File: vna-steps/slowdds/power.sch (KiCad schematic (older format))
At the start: 13 parts

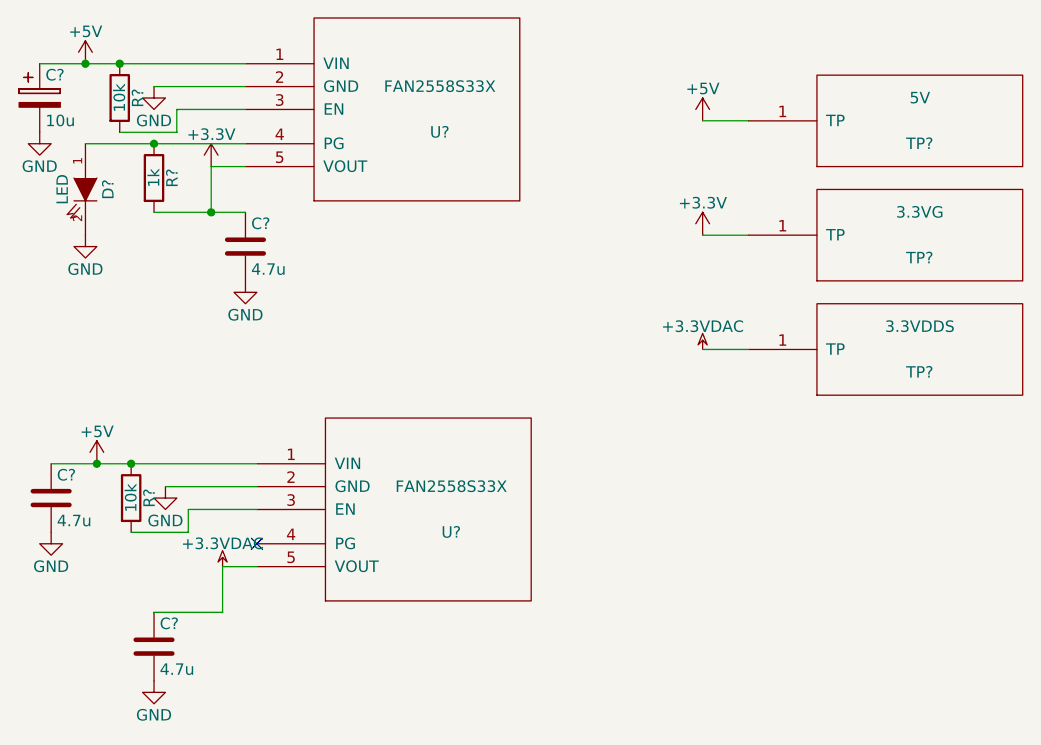
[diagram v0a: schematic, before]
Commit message: slowdds layout completed. images + schematics generated. ZIP file scripts added and documented in README. slowdds gerbers generated + zipped.
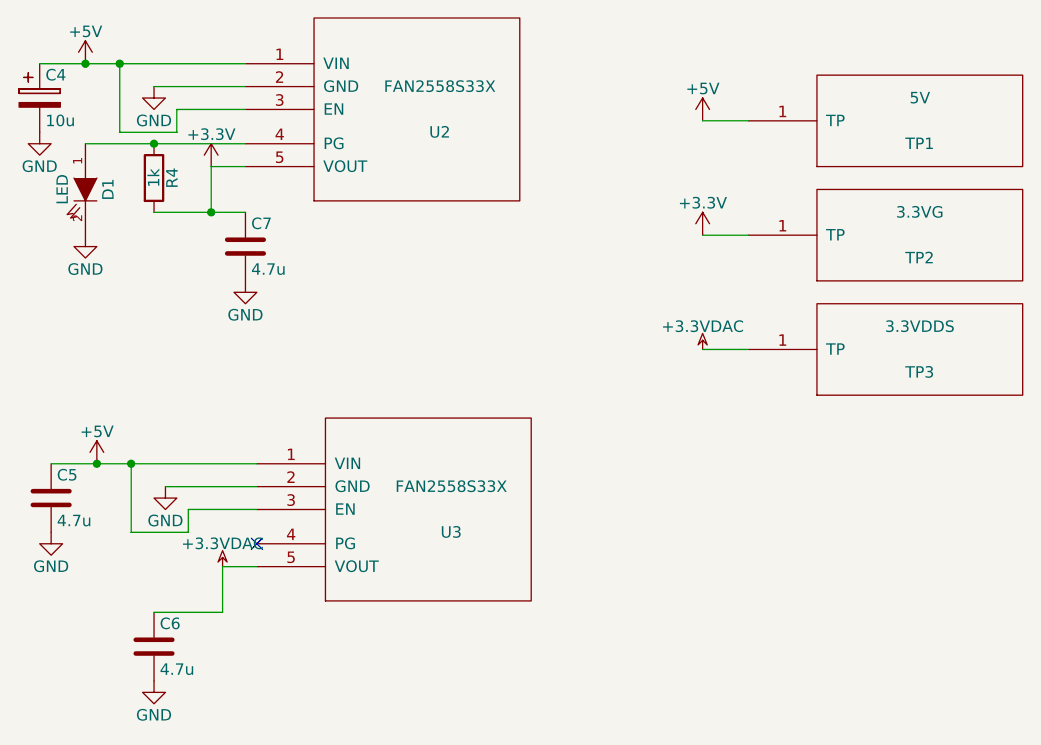
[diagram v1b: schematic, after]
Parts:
- removed R? (x2): 10k, symbol R
- C4: renamed from C?; footprint (none) -> Capacitors_Tantalum_SMD:TantalC_SizeA_EIA-3216_Reflow
- C5, C6, C7: renamed from C?; footprint (none) -> Capacitors_SMD:C_0603
- D1: renamed from D?; footprint (none) -> LEDs:LED-0603
- R4: renamed from R?; footprint (none) -> Resistors_SMD:R_0402
- TP1, TP2, TP3: renamed from TP?; footprint MODULE -> bce:TP
- U2, U3: renamed from U?; footprint MODULE -> Housings_SOT-23_SOT-143_TSOT-6:SOT-23-5
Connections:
- net +5V: now also U2.3 (EN), U3.3 (EN)
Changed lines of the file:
@@
 $EndDescr
 $Comp
-L GND #PWR?
+L GND #PWR011
 U 1 1 55851E90
 P 3750 3300
-F 0 "#PWR?" H 3750 3050 50  0001 C CNN
+F 0 "#PWR011" H 3750 3050 50  0001 C CNN
 F 1 "GND" H 3750 3150 50  0000 C CNN
 F 2 "" H 3750 3300 60  0000 C CNN
@@
 Connection ~ 3600 3000
 $Comp
-L C C?
+L C C7
 U 1 1 55851DEA
 P 3750 3150
-F 0 "C?" H 3775 3250 50  0000 L CNN
+F 0 "C7" H 3775 3250 50  0000 L CNN
 F 1 "4.7u" H 3775 3050 50  0000 L CNN
-F 2 "" H 3788 3000 30  0000 C CNN
+F 2 "Capacitors_SMD:C_0603" H 3788 3000 30  0001 C CNN
 F 3 "" H 3750 3150 60  0000 C CNN
 	1    3750 3150
@@
 $EndComp
 $Comp
-L GND #PWR?
+L GND #PWR012
 U 1 1 55851DC9
 P 2850 2650
-F 0 "#PWR?" H 2850 2400 50  0001 C CNN
+F 0 "#PWR012" H 2850 2400 50  0001 C CNN
 F 1 "GND" H 2850 2500 50  0000 C CNN
 F 2 "" H 2850 2650 60  0000 C CNN
@@
 	3350 2450 3750 2450
 $Comp
-L GND #PWR?
+L GND #PWR013
 U 1 1 55851D93
 P 3050 3100
-F 0 "#PWR?" H 3050 2850 50  0001 C CNN
+F 0 "#PWR013" H 3050 2850 50  0001 C CNN
 F 1 "GND" H 3050 2950 50  0000 C CNN
 F 2 "" H 3050 3100 60  0000 C CNN
@@
 Connection ~ 3350 2700
 $Comp
-L LED D?
+L LED D1
 U 1 1 55851CDF
 P 3050 2900
-F 0 "D?" H 3050 3000 50  0000 C CNN
+F 0 "D1" H 3050 3000 50  0000 C CNN
 F 1 "LED" H 3050 2800 50  0000 C CNN
-F 2 "" H 3050 2900 60  0000 C CNN
+F 2 "LEDs:LED-0603" H 3050 2900 60  0001 C CNN
 F 3 "" H 3050 2900 60  0000 C CNN
 	1    3050 2900
@@
 	3600 3000 3600 2800
 Wire Wire Line
-	3350 3000 3600 3000
-Wire Wire Line
-	3600 3000 3750 3000
-Wire Wire Line
-	3050 2700 3350 2700
-Wire Wire Line
-	3350 2700 3750 2700
-$Comp
-L R R?
+	3350 3000 3750 3000
+Wire Wire Line
+	3050 2700 3750 2700
+$Comp
+L R R4
 U 1 1 55851C98
 P 3350 2850
-F 0 "R?" V 3430 2850 50  0000 C CNN
+F 0 "R4" V 3430 2850 50  0000 C CNN
 F 1 "1k" V 3350 2850 50  0000 C CNN
-F 2 "" V 3280 2850 30  0000 C CNN
+F 2 "Resistors_SMD:R_0402" V 3280 2850 30  0001 C CNN
 F 3 "" H 3350 2850 30  0000 C CNN
 	1    3350 2850
@@
 	3600 2800 3750 2800
 $Comp
-L +3.3V #PWR?
+L +3.3V #PWR014
 U 1 1 55851C32
 P 3600 2800
-F 0 "#PWR?" H 3600 2650 50  0001 C CNN
+F 0 "#PWR014" H 3600 2650 50  0001 C CNN
 F 1 "+3.3V" H 3600 2940 50  0000 C CNN
 F 2 "" H 3600 2800 60  0000 C CNN
@@
 $EndComp
 $Comp
-L GND #PWR?
+L GND #PWR015
 U 1 1 55851BFD
 P 3350 2450
-F 0 "#PWR?" H 3350 2200 50  0001 C CNN
+F 0 "#PWR015" H 3350 2200 50  0001 C CNN
 F 1 "GND" H 3350 2300 50  0000 C CNN
 F 2 "" H 3350 2450 60  0000 C CNN
@@
 Connection ~ 3050 2350
 Wire Wire Line
-	2850 2350 3050 2350
-Wire Wire Line
-	3050 2350 3200 2350
-Wire Wire Line
-	3200 2350 3750 2350
-$Comp
-L R R?
-U 1 1 55851B9B
-P 3200 2500
-F 0 "R?" V 3280 2500 50  0000 C CNN
-F 1 "10k" V 3200 2500 50  0000 C CNN
-F 2 "" V 3130 2500 30  0000 C CNN
-F 3 "" H 3200 2500 30  0000 C CNN
-	1    3200 2500
-	1    0    0    -1
-$EndComp
-$Comp
-L +5V #PWR?
+	2850 2350 3750 2350
+$Comp
+L +5V #PWR016
 U 1 1 55851B85
 P 3050 2350
-F 0 "#PWR?" H 3050 2200 50  0001 C CNN
+F 0 "#PWR016" H 3050 2200 50  0001 C CNN
 F 1 "+5V" H 3050 2490 50  0000 C CNN
 F 2 "" H 3050 2350 60  0000 C CNN
@@
 $EndComp
 $Comp
-L CP C?
+L CP C4
 U 1 1 55851B48
 P 2850 2500
-F 0 "C?" H 2875 2600 50  0000 L CNN
+F 0 "C4" H 2875 2600 50  0000 L CNN
 F 1 "10u" H 2875 2400 50  0000 L CNN
-F 2 "" H 2888 2350 30  0000 C CNN
+F 2 "Capacitors_Tantalum_SMD:TantalC_SizeA_EIA-3216_Reflow" H 2888 2350 30  0001 C CNN
 F 3 "" H 2850 2500 60  0000 C CNN
 	1    2850 2500
@@
 $EndComp
 $Comp
-L FAN2558S33X U?
+L FAN2558S33X U2
 U 1 1 55851B19
 P 4500 2550
-F 0 "U?" H 4600 2450 50  0000 C CNN
+F 0 "U2" H 4600 2450 50  0000 C CNN
 F 1 "FAN2558S33X" H 4600 2650 50  0000 C CNN
-F 2 "MODULE" H 4500 2200 50  0001 C CNN
+F 2 "Housings_SOT-23_SOT-143_TSOT-6:SOT-23-5" H 4500 2200 50  0001 C CNN
 F 3 "DOCUMENTATION" H 4500 2850 50  0001 C CNN
 	1    4500 2550
@@
 $EndComp
 $Comp
-L GND #PWR?
+L GND #PWR017
 U 1 1 558520FF
 P 3350 5050
-F 0 "#PWR?" H 3350 4800 50  0001 C CNN
+F 0 "#PWR017" H 3350 4800 50  0001 C CNN
 F 1 "GND" H 3350 4900 50  0000 C CNN
 F 2 "" H 3350 5050 60  0000 C CNN
@@
 $EndComp
 $Comp
-L C C?
+L C C6
 U 1 1 55852106
 P 3350 4900
-F 0 "C?" H 3375 5000 50  0000 L CNN
+F 0 "C6" H 3375 5000 50  0000 L CNN
 F 1 "4.7u" H 3375 4800 50  0000 L CNN
-F 2 "" H 3388 4750 30  0000 C CNN
+F 2 "Capacitors_SMD:C_0603" H 3388 4750 30  0001 C CNN
 F 3 "" H 3350 4900 60  0000 C CNN
 	1    3350 4900
@@
 $EndComp
 $Comp
-L GND #PWR?
+L GND #PWR018
 U 1 1 5585210C
 P 2900 4400
-F 0 "#PWR?" H 2900 4150 50  0001 C CNN
+F 0 "#PWR018" H 2900 4150 50  0001 C CNN
 F 1 "GND" H 2900 4250 50  0000 C CNN
 F 2 "" H 2900 4400 60  0000 C CNN
@@
 	3650 4550 3800 4550
 $Comp
-L GND #PWR?
+L GND #PWR019
 U 1 1 55852130
 P 3400 4200
-F 0 "#PWR?" H 3400 3950 50  0001 C CNN
+F 0 "#PWR019" H 3400 3950 50  0001 C CNN
 F 1 "GND" H 3400 4050 50  0000 C CNN
 F 2 "" H 3400 4200 60  0000 C CNN
@@
 Connection ~ 3100 4100
 Wire Wire Line
-	2900 4100 3100 4100
-Wire Wire Line
-	3100 4100 3250 4100
-Wire Wire Line
-	3250 4100 3800 4100
-$Comp
-L R R?
-U 1 1 5585213C
-P 3250 4250
-F 0 "R?" V 3330 4250 50  0000 C CNN
-F 1 "10k" V 3250 4250 50  0000 C CNN
-F 2 "" V 3180 4250 30  0000 C CNN
-F 3 "" H 3250 4250 30  0000 C CNN
-	1    3250 4250
-	1    0    0    -1
-$EndComp
-$Comp
-L +5V #PWR?
+	2900 4100 3800 4100
+$Comp
+L +5V #PWR020
 U 1 1 55852142
 P 3100 4100
-F 0 "#PWR?" H 3100 3950 50  0001 C CNN
+F 0 "#PWR020" H 3100 3950 50  0001 C CNN
 F 1 "+5V" H 3100 4240 50  0000 C CNN
 F 2 "" H 3100 4100 60  0000 C CNN
@@
 $EndComp
 $Comp
-L FAN2558S33X U?
+L FAN2558S33X U3
 U 1 1 5585214E
 P 4550 4300
-F 0 "U?" H 4650 4200 50  0000 C CNN
+F 0 "U3" H 4650 4200 50  0000 C CNN
 F 1 "FAN2558S33X" H 4650 4400 50  0000 C CNN
-F 2 "MODULE" H 4550 3950 50  0001 C CNN
+F 2 "Housings_SOT-23_SOT-143_TSOT-6:SOT-23-5" H 4550 3950 50  0001 C CNN
 F 3 "DOCUMENTATION" H 4550 4600 50  0001 C CNN
 	1    4550 4300
@@
 $EndComp
 $Comp
-L TP TP?
+L TP TP1
 U 1 1 558521CE
 P 6700 2600
-F 0 "TP?" H 6700 2500 50  0000 C CNN
+F 0 "TP1" H 6700 2500 50  0000 C CNN
 F 1 "5V" H 6700 2700 50  0000 C CNN
-F 2 "MODULE" H 6450 2450 50  0001 C CNN
+F 2 "bce:TP" H 6450 2450 50  0001 C CNN
 F 3 "DOCUMENTATION" H 6700 2600 50  0001 C CNN
 	1    6700 2600
@@
 $EndComp
 $Comp
-L TP TP?
+L TP TP2
 U 1 1 55852299
 P 6700 3100
-F 0 "TP?" H 6700 3000 50  0000 C CNN
+F 0 "TP2" H 6700 3000 50  0000 C CNN
 F 1 "3.3VG" H 6700 3200 50  0000 C CNN
-F 2 "MODULE" H 6450 2950 50  0001 C CNN
+F 2 "bce:TP" H 6450 2950 50  0001 C CNN
 F 3 "DOCUMENTATION" H 6700 3100 50  0001 C CNN
 	1    6700 3100
@@
 $EndComp
 $Comp
-L TP TP?
+L TP TP3
 U 1 1 55852361
 P 6700 3600
-F 0 "TP?" H 6700 3500 50  0000 C CNN
+F 0 "TP3" H 6700 3500 50  0000 C CNN
 F 1 "3.3VDDS" H 6700 3700 50  0000 C CNN
-F 2 "MODULE" H 6450 3450 50  0001 C CNN
+F 2 "bce:TP" H 6450 3450 50  0001 C CNN
 F 3 "DOCUMENTATION" H 6700 3600 50  0001 C CNN
 	1    6700 3600
@@
 $EndComp
 $Comp
-L +5V #PWR?
+L +5V #PWR021
 U 1 1 5585254A
 P 5750 2600
-F 0 "#PWR?" H 5750 2450 50  0001 C CNN
+F 0 "#PWR021" H 5750 2450 50  0001 C CNN
 F 1 "+5V" H 5750 2740 50  0000 C CNN
 F 2 "" H 5750 2600 60  0000 C CNN
@@
 $EndComp
 $Comp
-L +3.3V #PWR?
+L +3.3V #PWR022
 U 1 1 5585256D
 P 5750 3100
-F 0 "#PWR?" H 5750 2950 50  0001 C CNN
+F 0 "#PWR022" H 5750 2950 50  0001 C CNN
 F 1 "+3.3V" H 5750 3240 50  0000 C CNN
 F 2 "" H 5750 3100 60  0000 C CNN
@@
 $EndComp
 $Comp
-L +3.3VDAC #PWR?
+L +3.3VDAC #PWR023
 U 1 1 55852608
 P 5750 3600
-F 0 "#PWR?" H 5900 3550 50  0001 C CNN
+F 0 "#PWR023" H 5900 3550 50  0001 C CNN
 F 1 "+3.3VDAC" H 5750 3700 50  0000 C CNN
 F 2 "" H 5750 3600 60  0000 C CNN
@@
 	5750 2600 5950 2600
 $Comp
-L +3.3VDAC #PWR?
+L +3.3VDAC #PWR024
 U 1 1 55852700
 P 3650 4550
-F 0 "#PWR?" H 3800 4500 50  0001 C CNN
+F 0 "#PWR024" H 3800 4500 50  0001 C CNN
 F 1 "+3.3VDAC" H 3650 4650 50  0000 C CNN
 F 2 "" H 3650 4550 60  0000 C CNN
@@
 $EndComp
 $Comp
-L C C?
+L C C5
 U 1 1 55852830
 P 2900 4250
-F 0 "C?" H 2925 4350 50  0000 L CNN
+F 0 "C5" H 2925 4350 50  0000 L CNN
 F 1 "4.7u" H 2925 4150 50  0000 L CNN
-F 2 "" H 2938 4100 30  0000 C CNN
+F 2 "Capacitors_SMD:C_0603" H 2938 4100 30  0001 C CNN
 F 3 "" H 2900 4250 60  0000 C CNN
 	1    2900 4250
@@
 $EndComp
 NoConn ~ 3800 4450
+Wire Wire Line
+	3200 2650 3200 2350
+Wire Wire Line
+	3250 4400 3250 4100
 $EndSCHEMATC
